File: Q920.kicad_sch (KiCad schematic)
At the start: 12 parts, among them J1 入力側 USB_A, J2 XH-B4B, J3 出力側 USB_A, J4 SW pin/Conn_01x02_Socket, J5 TEST POINT, J6 XH-4, K1 SRD-05VDC-SL-C, K2 SRD-05VDC-SL-C, U1 TLP222A

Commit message: PCB基板化
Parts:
- removed K1, K2: SRD-05VDC-SL-C, HOLLY:Relay_SPDT_Omron-G5LE-1, symbol Relay:Relay_SPDT
- added R3, R4: 68/1W, Resistor_THT:R_Axial_DIN0411_L9.9mm_D3.6mm_P15.24mm_Horizontal, symbol Device:R_US
- D1: value LED -> OSG8HA3Z74A; footprint (none) -> LED_THT:LED_D3.0mm
- J3: footprint (none) -> Connector_USB:USB_A_Stewart_SS-52100-001_Horizontal
- J4: footprint (none) -> Connector_JST:JST_XH_B2B-XH-A_1x02_P2.50mm_Vertical; symbol Connector:Conn_01x02_Socket -> Connector_Generic:Conn_01x02
- J5: footprint (none) -> Connector_PinSocket_2.54mm:PinSocket_1x04_P2.54mm_Vertical
- R1, R2: footprint (none) -> Resistor_THT:R_Axial_DIN0204_L3.6mm_D1.6mm_P7.62mm_Horizontal
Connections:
- net GND: now also R3.2, R4.2
- net at U1.3: now also R3.1, R4.1
- no-connect marks 6 -> 0
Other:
- moved on the sheet: J4

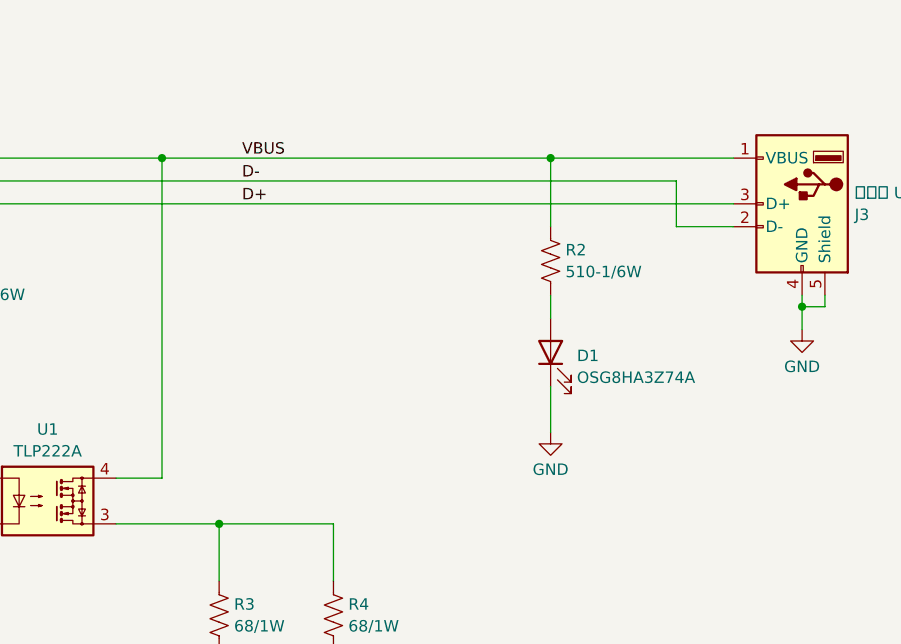
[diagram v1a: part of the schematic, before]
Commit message: cad: リレーを抵抗に変更した
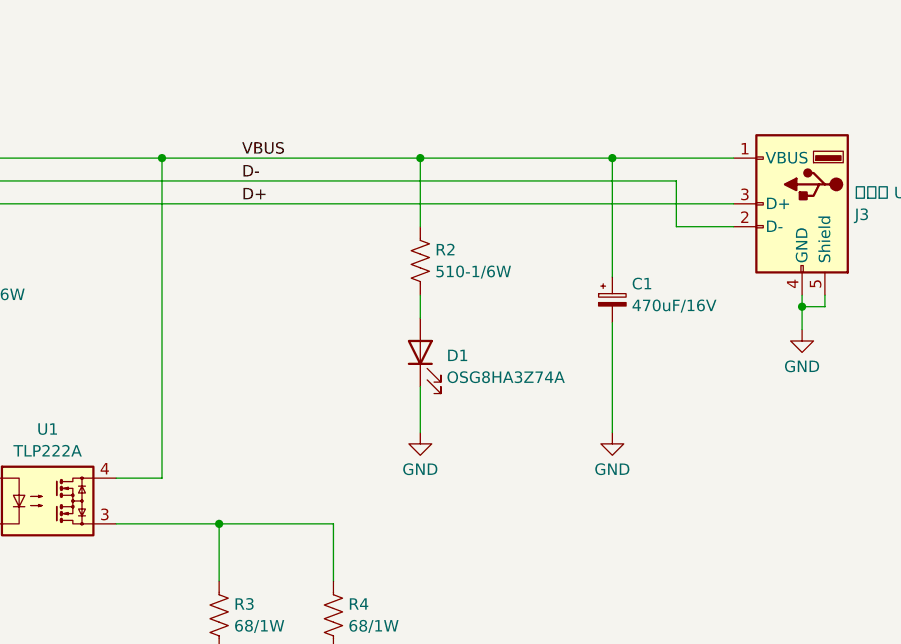
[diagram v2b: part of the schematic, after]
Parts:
- added C1: 470uF/16V, Capacitor_THT:CP_Radial_D8.0mm_P3.50mm, symbol Device:C_Polarized_Small
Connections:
- net GND: now also C1.2
- net VBUS: now also C1.1
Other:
- moved on the sheet: D1, R2
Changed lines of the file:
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@@
     (comment 1 "2.00: リレーから抵抗に変更")
   )
+  (junction (at 179.832 69.85) (diameter 0) (color 0 0 0 0)
+  )
   (junction (at 111.76 77.47) (diameter 0) (color 0 0 0 0)
   )
@@
   (junction (at 157.48 110.49) (diameter 0) (color 0 0 0 0)
   )
-  (junction (at 194.31 69.85) (diameter 0) (color 0 0 0 0)
-  )
   (junction (at 151.13 69.85) (diameter 0) (color 0 0 0 0)
   )
   (junction (at 106.68 72.39) (diameter 0) (color 0 0 0 0)
   )
+  (junction (at 201.168 69.85) (diameter 0) (color 0 0 0 0)
+  )
   (wire (pts (xy 222.25 85.09) (xy 222.25 86.36))
     (stroke (width 0) (type default))
@@
     (stroke (width 0) (type default))
   )
+  (wire (pts (xy 201.168 88.138) (xy 201.168 100.33))
+    (stroke (width 0) (type default))
+  )
   (wire (pts (xy 97.79 74.93) (xy 109.22 74.93))
     (stroke (width 0) (type default))
@@
     (stroke (width 0) (type default))
   )
-  (wire (pts (xy 151.13 69.85) (xy 194.31 69.85))
+  (wire (pts (xy 151.13 69.85) (xy 179.832 69.85))
     (stroke (width 0) (type default))
   )
@@
     (stroke (width 0) (type default))
   )
-  (wire (pts (xy 194.31 69.85) (xy 194.31 77.47))
+  (wire (pts (xy 179.832 69.85) (xy 179.832 77.47))
+    (stroke (width 0) (type default))
+  )
+  (wire (pts (xy 201.168 69.85) (xy 214.63 69.85))
     (stroke (width 0) (type default))
   )
@@
     (stroke (width 0) (type default))
   )
-  (wire (pts (xy 194.31 95.25) (xy 194.31 100.33))
-    (stroke (width 0) (type default))
-  )
-  (wire (pts (xy 194.31 85.09) (xy 194.31 87.63))
+  (wire (pts (xy 179.832 95.25) (xy 179.832 100.33))
+    (stroke (width 0) (type default))
+  )
+  (wire (pts (xy 179.832 85.09) (xy 179.832 87.63))
     (stroke (width 0) (type default))
   )
@@
     (stroke (width 0) (type default))
   )
-  (wire (pts (xy 194.31 69.85) (xy 214.63 69.85))
+  (wire (pts (xy 201.168 69.85) (xy 201.168 83.058))
+    (stroke (width 0) (type default))
+  )
+  (wire (pts (xy 179.832 69.85) (xy 201.168 69.85))
     (stroke (width 0) (type default))
   )
@@
     (effects (font (size 1.27 1.27)) (justify left bottom))
   )
-  (symbol (lib_id "Device:LED") (at 194.31 91.44 90) (unit 1)
-    (in_bom yes) (on_board yes) (dnp no) (fields_autoplaced)
-    (property "Reference" "D1" (at 197.231 91.8154 90)
+  (symbol (lib_id "Device:LED") (at 179.832 91.44 90) (unit 1)
+    (in_bom yes) (on_board yes) (dnp no) (fields_autoplaced)
+    (property "Reference" "D1" (at 182.753 91.8154 90)
       (effects (font (size 1.27 1.27)) (justify right))
     )
-    (property "Value" "OSG8HA3Z74A" (at 197.231 94.2396 90)
+    (property "Value" "OSG8HA3Z74A" (at 182.753 94.2396 90)
       (effects (font (size 1.27 1.27)) (justify right))
     )
-    (property "Footprint" "LED_THT:LED_D3.0mm" (at 194.31 91.44 0)
-      (effects (font (size 1.27 1.27)) hide)
-    )
-    (property "Datasheet" "https://akizukidenshi.com/download/ds/optosupply/OSG8HA3Z74A.pdf" (at 194.31 91.44 0)
+    (property "Footprint" "LED_THT:LED_D3.0mm" (at 179.832 91.44 0)
+      (effects (font (size 1.27 1.27)) hide)
+    )
+    (property "Datasheet" "https://akizukidenshi.com/download/ds/optosupply/OSG8HA3Z74A.pdf" (at 179.832 91.44 0)
       (effects (font (size 1.27 1.27)) hide)
     )
@@
     )
   )
-  (symbol (lib_id "power:GND") (at 194.31 100.33 0) (unit 1)
-    (in_bom yes) (on_board yes) (dnp no) (fields_autoplaced)
-    (property "Reference" "#PWR06" (at 194.31 106.68 0)
-      (effects (font (size 1.27 1.27)) hide)
-    )
-    (property "Value" "GND" (at 194.31 104.4631 0)
-      (effects (font (size 1.27 1.27)))
-    )
-    (property "Footprint" "" (at 194.31 100.33 0)
-      (effects (font (size 1.27 1.27)) hide)
-    )
-    (property "Datasheet" "" (at 194.31 100.33 0)
+  (symbol (lib_id "power:GND") (at 179.832 100.33 0) (unit 1)
+    (in_bom yes) (on_board yes) (dnp no) (fields_autoplaced)
+    (property "Reference" "#PWR06" (at 179.832 106.68 0)
+      (effects (font (size 1.27 1.27)) hide)
+    )
+    (property "Value" "GND" (at 179.832 104.4631 0)
+      (effects (font (size 1.27 1.27)))
+    )
+    (property "Footprint" "" (at 179.832 100.33 0)
+      (effects (font (size 1.27 1.27)) hide)
+    )
+    (property "Datasheet" "" (at 179.832 100.33 0)
       (effects (font (size 1.27 1.27)) hide)
     )
@@
     )
   )
-  (symbol (lib_id "Device:R_US") (at 194.31 81.28 0) (unit 1)
-    (in_bom yes) (on_board yes) (dnp no) (fields_autoplaced)
-    (property "Reference" "R2" (at 195.961 80.0679 0)
-      (effects (font (size 1.27 1.27)) (justify left))
-    )
-    (property "Value" "510-1/6W" (at 195.961 82.4921 0)
-      (effects (font (size 1.27 1.27)) (justify left))
-    )
-    (property "Footprint" "Resistor_THT:R_Axial_DIN0204_L3.6mm_D1.6mm_P7.62mm_Horizontal" (at 195.326 81.534 90)
-      (effects (font (size 1.27 1.27)) hide)
-    )
-    (property "Datasheet" "https://akizukidenshi.com/download/ds/faithful/cf.pdf" (at 194.31 81.28 0)
+  (symbol (lib_id "Device:R_US") (at 179.832 81.28 0) (unit 1)
+    (in_bom yes) (on_board yes) (dnp no) (fields_autoplaced)
+    (property "Reference" "R2" (at 181.483 80.0679 0)
+      (effects (font (size 1.27 1.27)) (justify left))
+    )
+    (property "Value" "510-1/6W" (at 181.483 82.4921 0)
+      (effects (font (size 1.27 1.27)) (justify left))
+    )
+    (property "Footprint" "Resistor_THT:R_Axial_DIN0204_L3.6mm_D1.6mm_P7.62mm_Horizontal" (at 180.848 81.534 90)
+      (effects (font (size 1.27 1.27)) hide)
+    )
+    (property "Datasheet" "https://akizukidenshi.com/download/ds/faithful/cf.pdf" (at 179.832 81.28 0)
       (effects (font (size 1.27 1.27)) hide)
     )
@@
         (path "/a25f858a-1e58-4759-a09e-d5b13ae1c0fe"
           (reference "#PWR02") (unit 1)
+        )
+      )
+    )
+  )
+  (symbol (lib_id "Device:C_Polarized_Small") (at 201.168 85.598 0) (unit 1)
+    (in_bom yes) (on_board yes) (dnp no) (fields_autoplaced)
+    (property "Reference" "C1" (at 203.327 83.8398 0)
+      (effects (font (size 1.27 1.27)) (justify left))
+    )
+    (property "Value" "470uF/16V" (at 203.327 86.264 0)
+      (effects (font (size 1.27 1.27)) (justify left))
+    )
+    (property "Footprint" "Capacitor_THT:CP_Radial_D8.0mm_P3.50mm" (at 201.168 85.598 0)
+      (effects (font (size 1.27 1.27)) hide)
+    )
+    (property "Datasheet" "~" (at 201.168 85.598 0)
+      (effects (font (size 1.27 1.27)) hide)
+    )
+    (pin "2")
+    (pin "1")
+    (instances
+      (project "Q920"
+        (path "/a25f858a-1e58-4759-a09e-d5b13ae1c0fe"
+          (reference "C1") (unit 1)
         )
       )
@@
         )
       )
+    )
+  )
+  (symbol (lib_id "power:GND") (at 201.168 100.33 0) (unit 1)
+    (in_bom yes) (on_board yes) (dnp no) (fields_autoplaced)
+    (property "Reference" "#PWR07" (at 201.168 106.68 0)
+      (effects (font (size 1.27 1.27)) hide)
+    )
+    (property "Value" "GND" (at 201.168 104.4631 0)
+      (effects (font (size 1.27 1.27)))
+    )
+    (property "Footprint" "" (at 201.168 100.33 0)
+      (effects (font (size 1.27 1.27)) hide)
+    )
+    (property "Datasheet" "" (at 201.168 100.33 0)
+      (effects (font (size 1.27 1.27)) hide)
+    )
+    (pin "1")
+    (instances
+      (project "Q920"
+        (path "/a25f858a-1e58-4759-a09e-d5b13ae1c0fe"
+          (reference "#PWR07") (unit 1)
+        )
+      )
